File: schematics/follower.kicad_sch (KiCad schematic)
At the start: 26 parts, among them M2 Motor, M3 Motor, Q1 TLE5206_2S, Q2 TLE5206_2S, SW5 Reset, U10 PIC32MX170F256B, U5 Tape_Left, U6 Tape_Middle, U7 Tape_Right, U8 Quadrature_Encoder, U9 Quadrature_Encoder

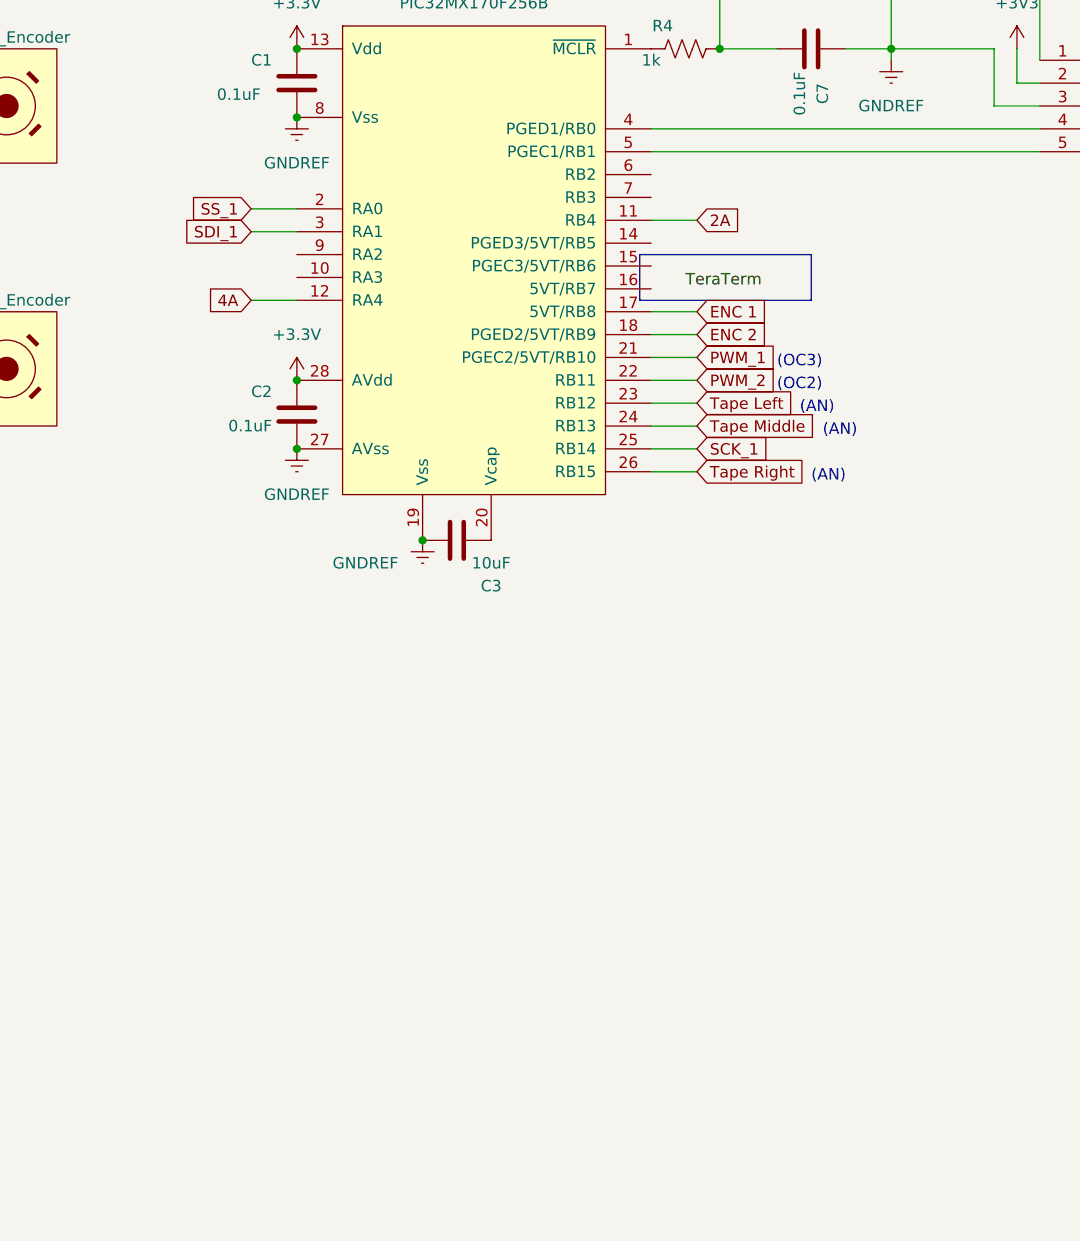
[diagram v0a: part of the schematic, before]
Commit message: Move IR sensors to follower PIC and add missing SPI PICs
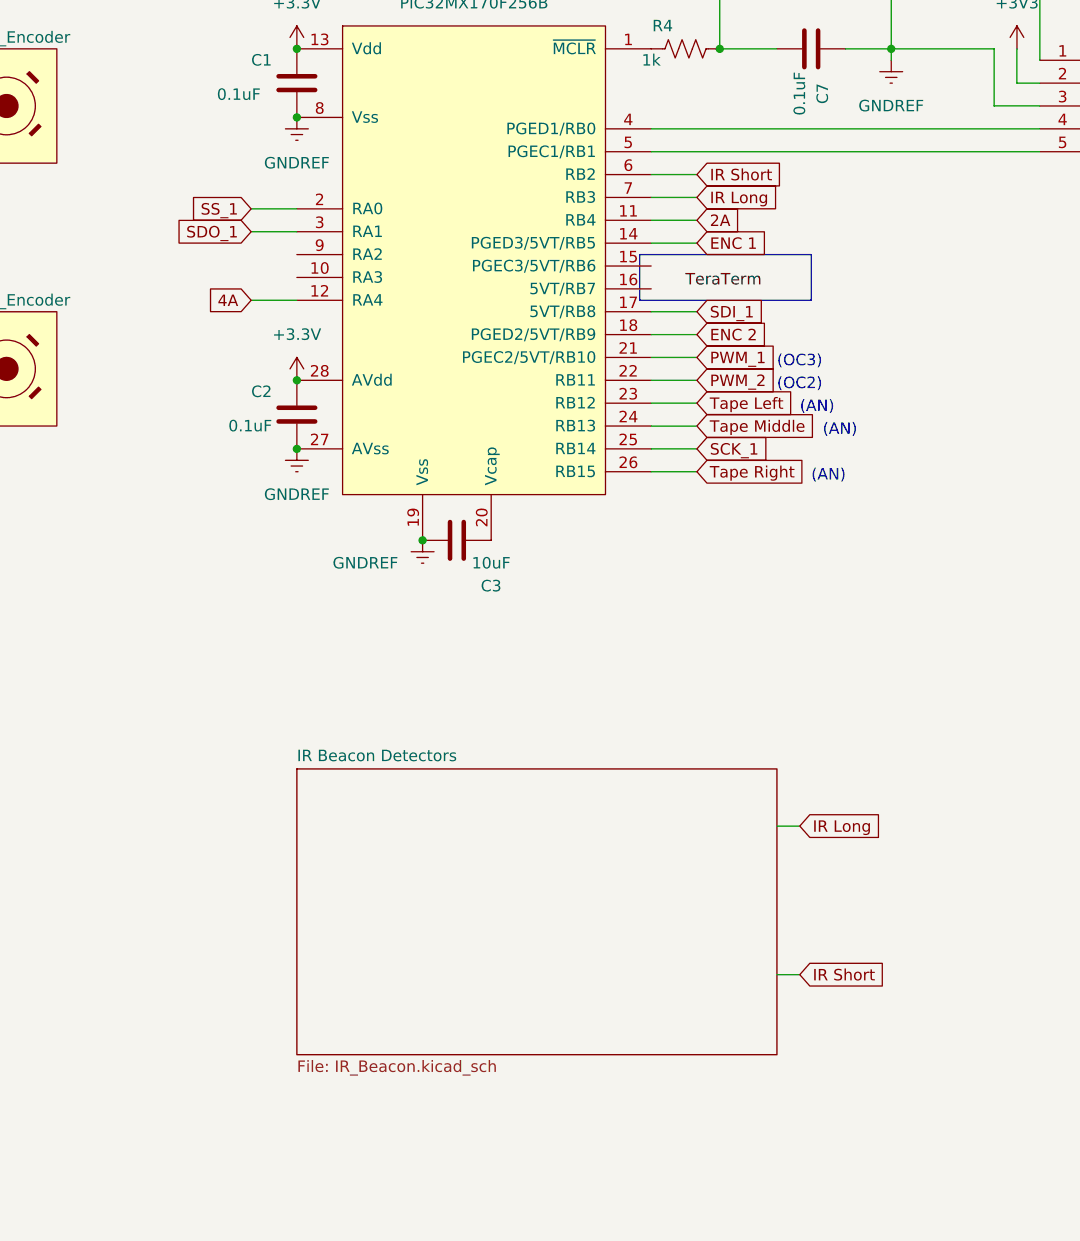
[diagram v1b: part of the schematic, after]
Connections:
- net ENC 1: now also U10.14 (PGED3/5VT/RB5); no longer U10.17 (5VT/RB8)
- net SDI_1: now also U10.17 (5VT/RB8); no longer U10.3 (RA1)
- net IR Short: now reaches U10.6 (RB2)
- net IR Long: now reaches U10.7 (RB3)
- new net SDO_1: U10.3 (RA1)
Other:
- added sheet IR Beacon Detectors (IR_Beacon.kicad_sch)
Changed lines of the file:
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@@
+    (stroke (width 0) (type default) (color 0 0 0 0))
+  )
+  (wire (pts (xy 226.06 121.92) (xy 228.6 121.92))
     (stroke (width 0) (type default) (color 0 0 0 0))
   )
@@
     (stroke (width 0) (type default) (color 0 0 0 0))
   )
+  (wire (pts (xy 226.06 138.43) (xy 228.6 138.43))
+    (stroke (width 0) (type default) (color 0 0 0 0))
+  )
   (wire (pts (xy 76.2 140.97) (xy 76.2 144.78))
     (stroke (width 0) (type default) (color 0 0 0 0))
@@
     (stroke (width 0) (type default) (color 0 0 0 0))
   )
+  (wire (pts (xy 74.93 78.74) (xy 76.2 78.74))
+    (stroke (width 0) (type default) (color 0 0 0 0))
+  )
+  (wire (pts (xy 99.06 63.5) (xy 99.06 66.04))
+    (stroke (width 0) (type default) (color 0 0 0 0))
+  )
+  (wire (pts (xy 59.69 74.93) (xy 59.69 77.47))
+    (stroke (width 0) (type default) (color 0 0 0 0))
+  )
+  (wire (pts (xy 63.5 36.83) (xy 104.14 36.83))
+    (stroke (width 0) (type default) (color 0 0 0 0))
+  )
+  (wire (pts (xy 29.21 69.85) (xy 36.83 69.85))
+    (stroke (width 0) (type default) (color 0 0 0 0))
+  )
+  (wire (pts (xy 87.63 76.2) (xy 86.36 76.2))
+    (stroke (width 0) (type default) (color 0 0 0 0))
+  )
+  (wire (pts (xy 212.09 46.99) (xy 255.27 46.99))
+    (stroke (width 0) (type default) (color 0 0 0 0))
+  )
+  (wire (pts (xy 76.2 63.5) (xy 74.93 63.5))
+    (stroke (width 0) (type default) (color 0 0 0 0))
+  )
+  (wire (pts (xy 34.29 66.04) (xy 34.29 40.64))
+    (stroke (width 0) (type default) (color 0 0 0 0))
+  )
+  (wire (pts (xy 74.93 38.1) (xy 74.93 50.8))
+    (stroke (width 0) (type default) (color 0 0 0 0))
+  )
   (wire (pts (xy 212.09 64.77) (xy 217.17 64.77))
     (stroke (width 0) (type default) (color 0 0 0 0))
   )
-  (wire (pts (xy 74.93 78.74) (xy 76.2 78.74))
-    (stroke (width 0) (type default) (color 0 0 0 0))
-  )
-  (wire (pts (xy 99.06 63.5) (xy 99.06 66.04))
-    (stroke (width 0) (type default) (color 0 0 0 0))
-  )
-  (wire (pts (xy 59.69 74.93) (xy 59.69 77.47))
-    (stroke (width 0) (type default) (color 0 0 0 0))
-  )
-  (wire (pts (xy 63.5 36.83) (xy 104.14 36.83))
-    (stroke (width 0) (type default) (color 0 0 0 0))
-  )
-  (wire (pts (xy 29.21 69.85) (xy 36.83 69.85))
-    (stroke (width 0) (type default) (color 0 0 0 0))
-  )
-  (wire (pts (xy 87.63 76.2) (xy 86.36 76.2))
-    (stroke (width 0) (type default) (color 0 0 0 0))
-  )
-  (wire (pts (xy 212.09 46.99) (xy 255.27 46.99))
-    (stroke (width 0) (type default) (color 0 0 0 0))
-  )
-  (wire (pts (xy 76.2 63.5) (xy 74.93 63.5))
-    (stroke (width 0) (type default) (color 0 0 0 0))
-  )
-  (wire (pts (xy 34.29 66.04) (xy 34.29 40.64))
-    (stroke (width 0) (type default) (color 0 0 0 0))
-  )
-  (wire (pts (xy 74.93 38.1) (xy 74.93 50.8))
-    (stroke (width 0) (type default) (color 0 0 0 0))
-  )
   (wire (pts (xy 69.85 144.78) (xy 76.2 144.78))
     (stroke (width 0) (type default) (color 0 0 0 0))
@@
     (stroke (width 0) (type default) (color 0 0 0 0))
   )
+  (wire (pts (xy 212.09 52.07) (xy 217.17 52.07))
+    (stroke (width 0) (type default) (color 0 0 0 0))
+  )
   (wire (pts (xy 53.34 41.91) (xy 59.69 41.91))
     (stroke (width 0) (type default) (color 0 0 0 0))
@@
     (stroke (width 0) (type default) (color 0 0 0 0))
   )
+  (wire (pts (xy 212.09 57.15) (xy 217.17 57.15))
+    (stroke (width 0) (type default) (color 0 0 0 0))
+  )
   (wire (pts (xy 29.21 44.45) (xy 36.83 44.45))
     (stroke (width 0) (type default) (color 0 0 0 0))
@@
   )
   (wire (pts (xy 76.2 171.45) (xy 76.2 168.91))
+    (stroke (width 0) (type default) (color 0 0 0 0))
+  )
+  (wire (pts (xy 212.09 49.53) (xy 217.17 49.53))
     (stroke (width 0) (type default) (color 0 0 0 0))
   )
@@
     )
   )
+  (global_label "ENC 1" (shape input) (at 217.17 57.15 0) (fields_autoplaced)
+    (effects (font (size 1.27 1.27)) (justify left))
+    (property "Intersheet References" "${INTERSHEET_REFS}" (id 0) (at 225.5098 57.2294 0)
+      (effects (font (size 1.27 1.27)) (justify left) hide)
+    )
+  )
   (global_label "Tape Left" (shape input) (at 50.8 118.11 180) (fields_autoplaced)
     (effects (font (size 1.27 1.27)) (justify right))
@@
     )
   )
+  (global_label "IR Short" (shape input) (at 228.6 138.43 0) (fields_autoplaced)
+    (effects (font (size 1.27 1.27)) (justify left))
+    (property "Intersheet References" "${INTERSHEET_REFS}" (id 0) (at 238.875 138.3506 0)
+      (effects (font (size 1.27 1.27)) (justify left) hide)
+    )
+  )
   (global_label "Tape Left" (shape input) (at 217.17 74.93 0) (fields_autoplaced)
     (effects (font (size 1.27 1.27)) (justify left))
@@
     )
   )
-  (global_label "SDI_1" (shape input) (at 167.64 55.88 180) (fields_autoplaced)
+  (global_label "SDO_1" (shape input) (at 167.64 55.88 180) (fields_autoplaced)
     (effects (font (size 1.27 1.27)) (justify right))
-    (property "Intersheet References" "${INTERSHEET_REFS}" (id 0) (at 159.9655 55.8006 0)
+    (property "Intersheet References" "${INTERSHEET_REFS}" (id 0) (at 159.2398 55.8006 0)
       (effects (font (size 1.27 1.27)) (justify right) hide)
+    )
+  )
+  (global_label "IR Long" (shape input) (at 228.6 121.92 0) (fields_autoplaced)
+    (effects (font (size 1.27 1.27)) (justify left))
+    (property "Intersheet References" "${INTERSHEET_REFS}" (id 0) (at 238.3307 121.8406 0)
+      (effects (font (size 1.27 1.27)) (justify left) hide)
+    )
+  )
+  (global_label "IR Short" (shape input) (at 217.17 49.53 0) (fields_autoplaced)
+    (effects (font (size 1.27 1.27)) (justify left))
+    (property "Intersheet References" "${INTERSHEET_REFS}" (id 0) (at 227.445 49.4506 0)
+      (effects (font (size 1.27 1.27)) (justify left) hide)
     )
   )
@@
     )
   )
+  (global_label "IR Long" (shape input) (at 217.17 52.07 0) (fields_autoplaced)
+    (effects (font (size 1.27 1.27)) (justify left))
+    (property "Intersheet References" "${INTERSHEET_REFS}" (id 0) (at 226.9007 51.9906 0)
+      (effects (font (size 1.27 1.27)) (justify left) hide)
+    )
+  )
+  (global_label "SDI_1" (shape input) (at 217.17 64.77 0) (fields_autoplaced)
+    (effects (font (size 1.27 1.27)) (justify left))
+    (property "Intersheet References" "${INTERSHEET_REFS}" (id 0) (at 224.8445 64.6906 0)
+      (effects (font (size 1.27 1.27)) (justify left) hide)
+    )
+  )
   (global_label "ENC 2" (shape input) (at 123.19 69.85 180) (fields_autoplaced)
     (effects (font (size 1.27 1.27)) (justify right))
     (property "Intersheet References" "${INTERSHEET_REFS}" (id 0) (at 114.8502 69.7706 0)
       (effects (font (size 1.27 1.27)) (justify right) hide)
-    )
-  )
-  (global_label "ENC 1" (shape input) (at 217.17 64.77 0) (fields_autoplaced)
-    (effects (font (size 1.27 1.27)) (justify left))
-    (property "Intersheet References" "${INTERSHEET_REFS}" (id 0) (at 225.5098 64.8494 0)
-      (effects (font (size 1.27 1.27)) (justify left) hide)
     )
   )
@@
     (pin "2")
   )
+  (sheet (at 172.72 115.57) (size 53.34 31.75) (fields_autoplaced)
+    (stroke (width 0.1524) (type solid) (color 0 0 0 0))
+    (fill (color 0 0 0 0.0000))
+    (property "Sheet name" "IR Beacon Detectors" (id 0) (at 172.72 114.8584 0)
+      (effects (font (size 1.27 1.27)) (justify left bottom))
+    )
+    (property "Sheet file" "IR_Beacon.kicad_sch" (id 1) (at 172.72 147.9046 0)
+      (effects (font (size 1.27 1.27)) (justify left top))
+    )
+  )
 )

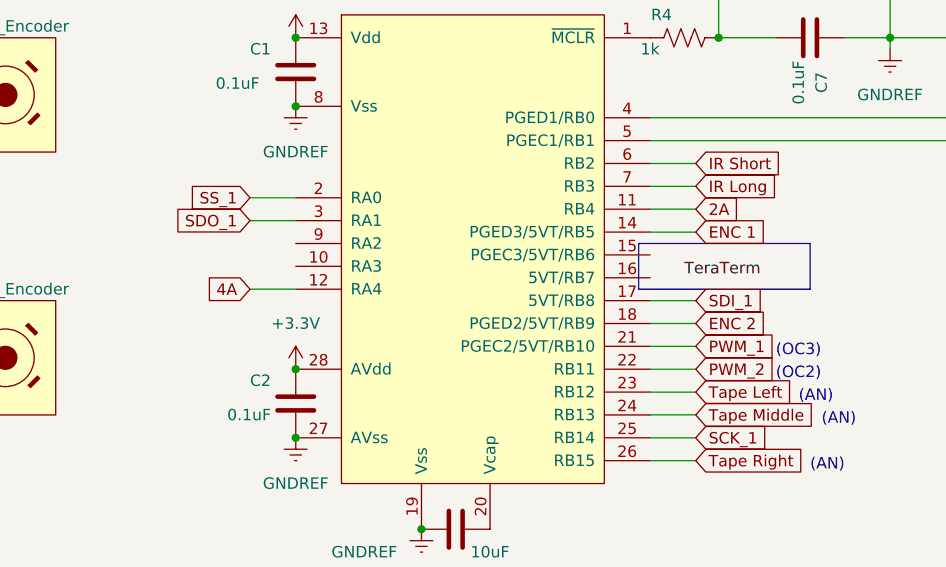
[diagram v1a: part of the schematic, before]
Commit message: Correct encoder pins on KiCad.
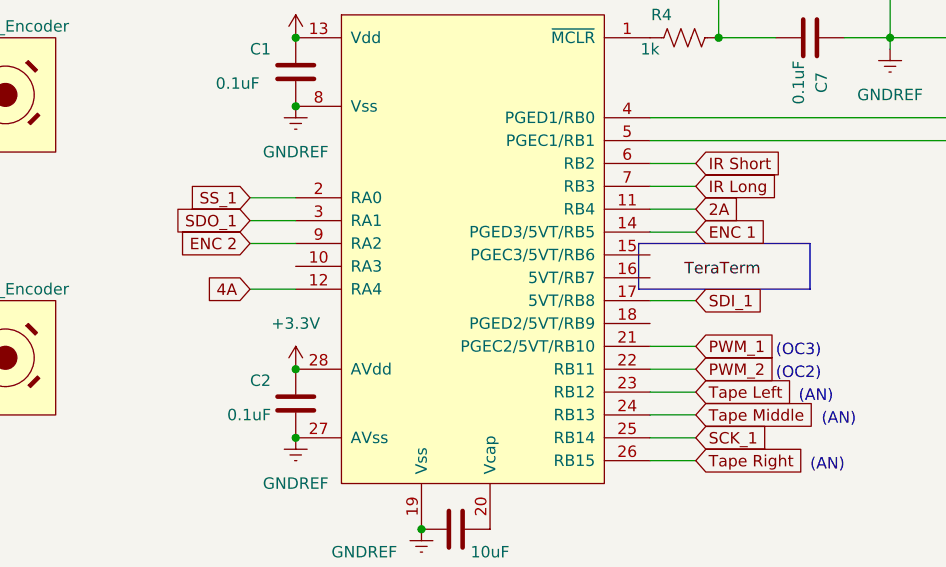
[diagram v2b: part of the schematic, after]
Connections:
- net ENC 2: now also U10.9 (RA2); no longer U10.18 (PGED2/5VT/RB9)
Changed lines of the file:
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@@
+    (stroke (width 0) (type default) (color 0 0 0 0))
+  )
+  (wire (pts (xy 167.64 58.42) (xy 172.72 58.42))
     (stroke (width 0) (type default) (color 0 0 0 0))
   )
@@
   )
   (wire (pts (xy 76.2 140.97) (xy 76.2 144.78))
-    (stroke (width 0) (type default) (color 0 0 0 0))
-  )
-  (wire (pts (xy 212.09 67.31) (xy 217.17 67.31))
     (stroke (width 0) (type default) (color 0 0 0 0))
   )
@@
     )
   )
-  (global_label "ENC 2" (shape input) (at 217.17 67.31 0) (fields_autoplaced)
-    (effects (font (size 1.27 1.27)) (justify left))
-    (property "Intersheet References" "${INTERSHEET_REFS}" (id 0) (at 225.5098 67.3894 0)
-      (effects (font (size 1.27 1.27)) (justify left) hide)
-    )
-  )
   (global_label "ENC 1" (shape input) (at 217.17 57.15 0) (fields_autoplaced)
     (effects (font (size 1.27 1.27)) (justify left))
@@
     )
   )
+  (global_label "ENC 2" (shape input) (at 167.64 58.42 180) (fields_autoplaced)
+    (effects (font (size 1.27 1.27)) (justify right))
+    (property "Intersheet References" "${INTERSHEET_REFS}" (id 0) (at 159.3002 58.3406 0)
+      (effects (font (size 1.27 1.27)) (justify right) hide)
+    )
+  )
